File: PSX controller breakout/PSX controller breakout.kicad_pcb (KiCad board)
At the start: 2 copper layers, 30 x 40 mm, 3 parts, among them J1 PSX Controller 1P, J2 JST-PH, J3 Conn_01x09_Pin

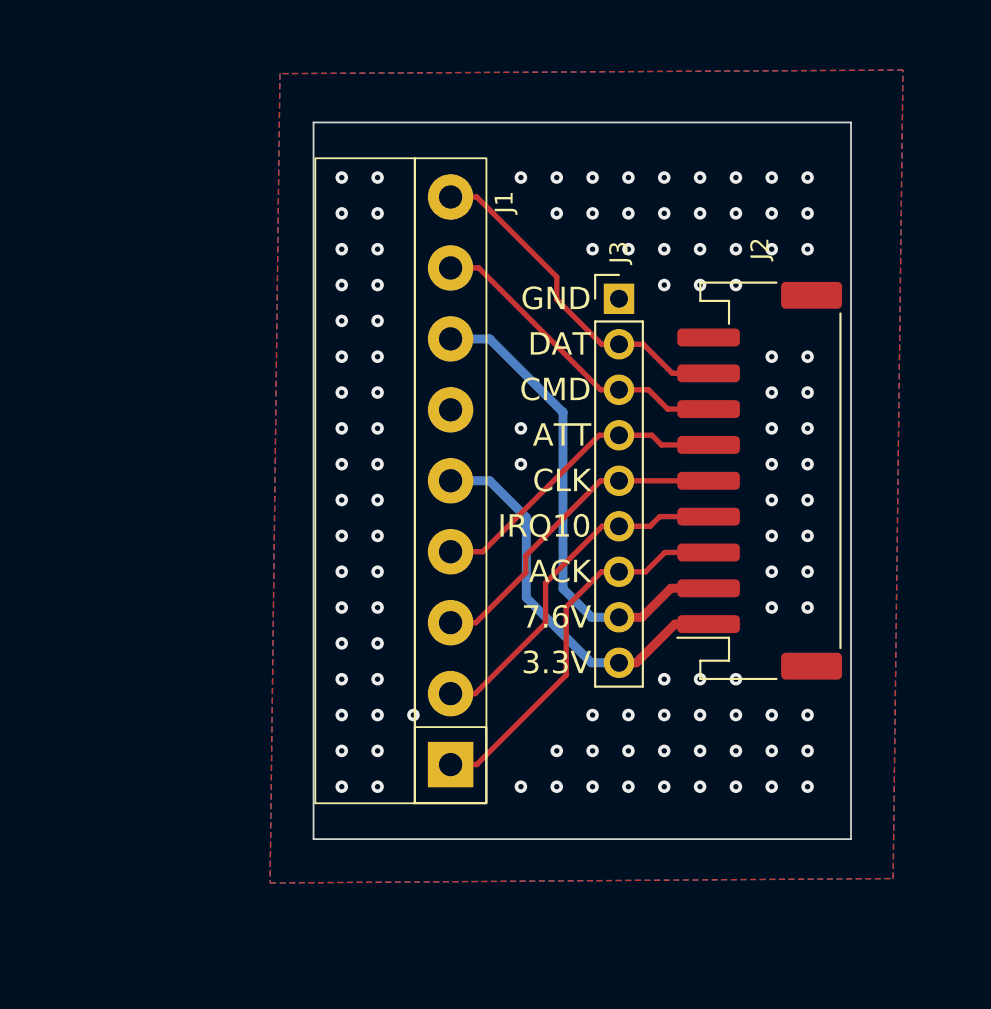
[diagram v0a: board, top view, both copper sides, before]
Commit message: Assigned PSX footprint and started layout
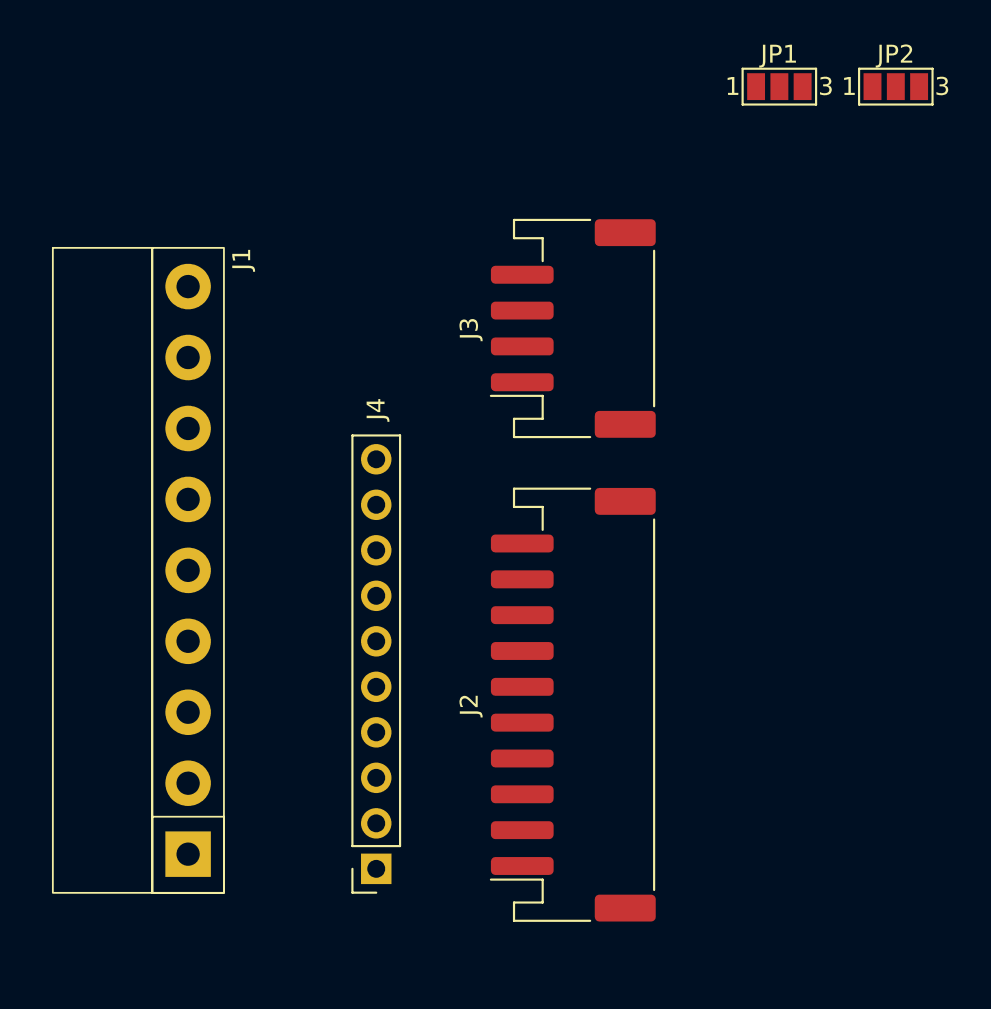
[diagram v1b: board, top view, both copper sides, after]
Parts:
- added J4: Conn_01x10_Pin, Connector_PinSocket_2.54mm:PinSocket_1x10_P2.54mm_Vertical, F.Cu at (128.5, 121.7)
- added JP1: Jumper_3_Open, Jumper:SolderJumper-3_P1.3mm_Open_Pad1.0x1.5mm_NumberLabels, F.Cu at (151.0, 78.0)
- added JP2: Jumper_3_Open, Jumper:SolderJumper-3_P1.3mm_Open_Pad1.0x1.5mm_NumberLabels, F.Cu at (157.5, 78.0)
- J1: value PSX Controller 1P -> PSX Connector 1P; footprint Nick_Connectors:PlayStation 1P -> Penny_Connectors:PSX Connector 1P
- J2: value JST-PH -> Conn_01x10_MountingPin; footprint Connector_JST:JST_PH_S9B-PH-SM4-TB_1x09-1MP_P2.00mm_Horizontal -> Connector_JST:JST_PH_S10B-PH-SM4-TB_1x10-1MP_P2.00mm_Horizontal
- J3: value Conn_01x09_Pin -> Conn_01x04_MountingPin; footprint Connector_PinHeader_2.54mm:PinHeader_1x09_P2.54mm_Vertical -> Connector_JST:JST_PH_S4B-PH-SM4-TB_1x04-1MP_P2.00mm_Horizontal
- moved J2 16.3 mm to (139.5, 112.5)
- moved J1 15.5 mm to (118.0, 105.0), turned to 0 degrees
- moved J3 3.04 mm to (139.5, 91.5), turned to 90 degrees
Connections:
- J1 pad 4: /ATT -> /ATT1_2
- J2 pad 1: +3.3V -> +7.6V
- J2 pad 2: +7.6V -> +3.3V
- J2 pad 3: /ACK -> /ATT1
- J2 pad 4: /IRQ10 -> /ATT2
- J2 pad 6: /ATT -> /DAT
- J2 pad 7: /CMD -> /ACK
- J2 pad 8: /DAT -> /CMD
- J2 pad 9: GND -> /IRQ10
- J3 pad 1: GND -> +7.6V
- J3 pad 2: /DAT -> +3.3V
- J3 pad 3: /CMD -> Net-(J3-Pin_3)
- J3 pad 4: /ATT -> GND
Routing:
- net +7.6V: track 27.3 -> 0.00 mm
- net +3.3V: track 22.1 -> 0.00 mm
- net /ACK: track 21.5 -> 0.00 mm
- net /IRQ10: track 19.8 -> 0.00 mm
- net /DAT: track 19.2 -> 0.00 mm
- net /CLK: track 18.2 -> 0.00 mm
- net /CMD: track 17.7 -> 0.00 mm
- net /ATT: track 17.3 -> 0.00 mm
- net GND: vias 109 -> 0
- removed copper zone on B.Cu, net GND
- removed copper zone on F.Cu, net GND
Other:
- board outline removed
- board text removed: "3.3V"
- board text removed: "7.6V"
- board text removed: "ACK"
- board text removed: "ATT"
- board text removed: "CLK"
- board text removed: "CMD"
- board text removed: "DAT"
- board text removed: "GND"
- board text removed: "IRQ10"
- board text removed: "PSX JST EDU v1"

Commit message: competed initial routing of PCB
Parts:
- JP1, JP2: moved to B.Cu
- moved JP1 30.4 mm to (123.3, 90.5)
- moved JP2 30.2 mm to (130.0, 90.5)
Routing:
- net +3.3V: track 0.00 -> 77.0 mm
- net +7.6V: track 0.00 -> 74.8 mm
- net /DAT: track 0.00 -> 49.4 mm
- net /ATT1: track 0.00 -> 40.0 mm, vias 0 -> 1
- net /CMD: track 0.00 -> 39.9 mm
- net /ATT2: track 0.00 -> 34.6 mm, vias 0 -> 1
- net /IRQ10: track 0.00 -> 32.6 mm
- net /ACK: track 0.00 -> 31.2 mm
- net /ATT1_2: track 0.00 -> 27.5 mm
- net /CLK: track 0.00 -> 20.1 mm
- net Net-(J3-Pin_3): track 0.00 -> 5.35 mm, vias 0 -> 1
- net Net-(JP1-B): track 0.00 -> 4.10 mm
- added copper zone on B.Cu, net GND
- added copper zone on F.Cu, net GND
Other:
- board outline added: 34.6 x 42 mm

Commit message: competed layout
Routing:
- net GND: vias 0 -> 95
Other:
- board text added: "P1"
- board text added: "P2"
- board text added: "PSX BREAKOUT PROTO REV 1"
